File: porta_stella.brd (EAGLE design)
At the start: 113.5 x 67.5 mm, 106 parts, among them CN4 MicroUSB, IC1 74LS00D, J1 PJ-393, T1 2N3904, T2 PN3906, T3 PN3906, T4 PN3906, T5 MMUN2133LT1G, U1 TPS61090RSAR, U2 MCP73871, X1 SSW-112-02-G-Q

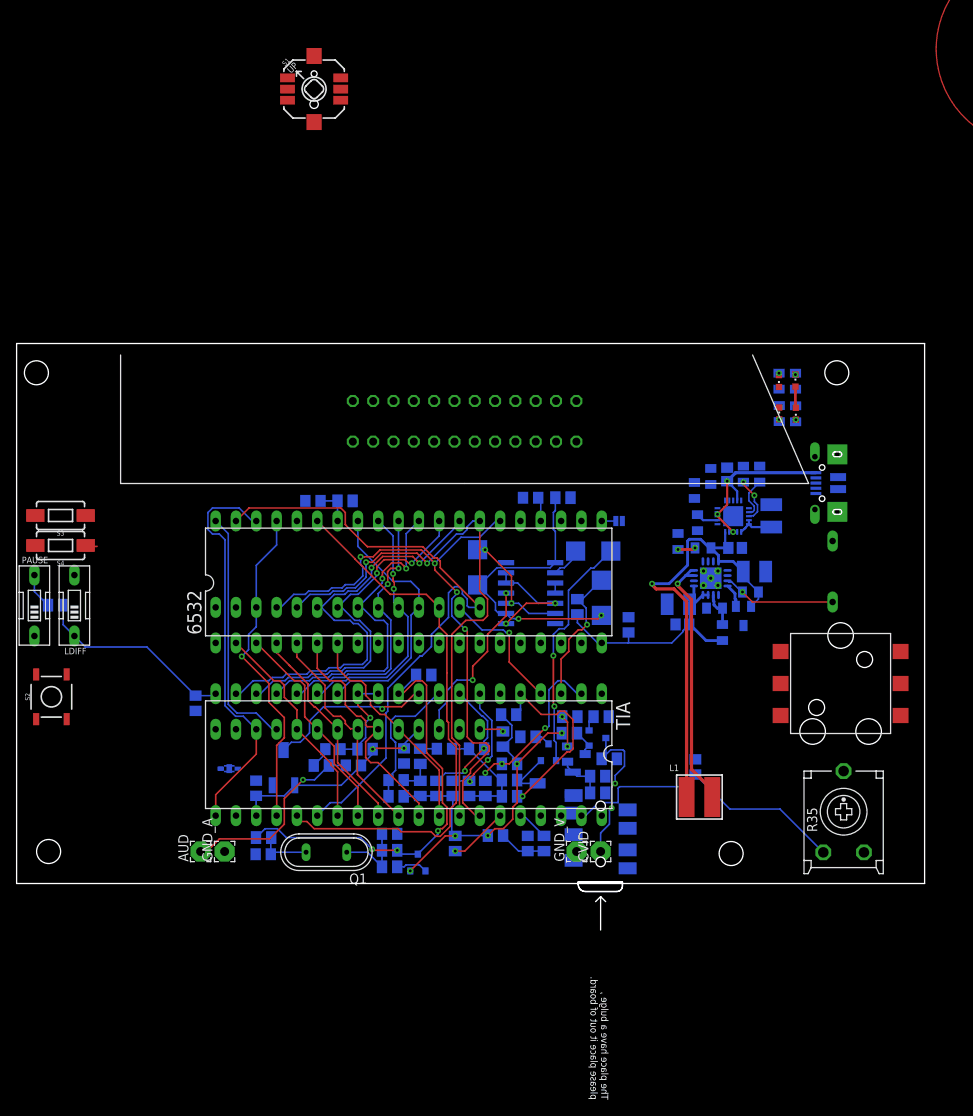
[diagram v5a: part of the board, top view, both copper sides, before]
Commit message: switched to gameboy form factor
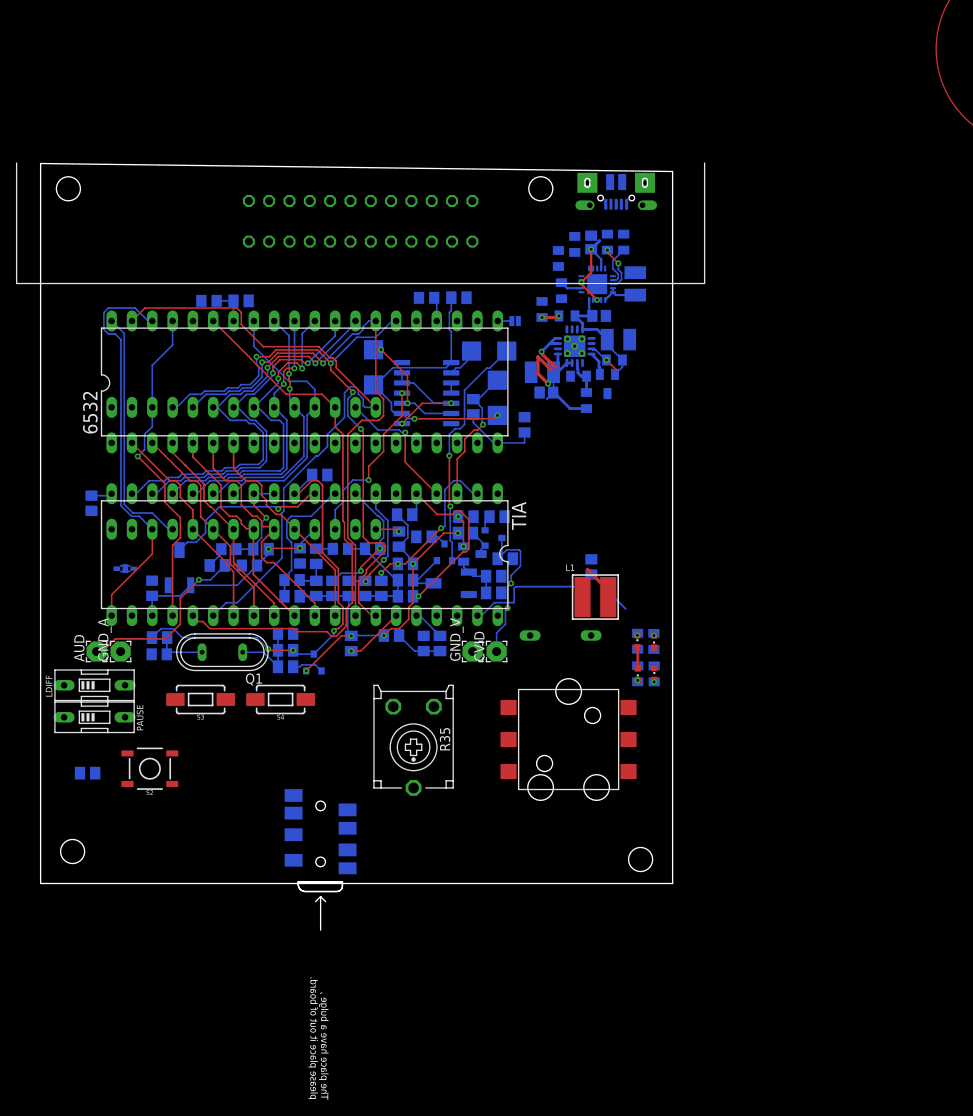
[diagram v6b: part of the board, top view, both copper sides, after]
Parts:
- removed S1: (no value), SparkFun-Switches:JOYSTICK_MINI
- moved R35 54.4 mm to (49.6, 17.0), turned to 180 degrees
- moved CN4 44.0 mm to (74.9, 85.7), turned to 180 degrees
- moved DONE 41.7 mm to (77.6, 26.1), turned to 180 degrees
- moved R45 41.6 mm to (77.6, 26.2), turned to 270 degrees
- moved ON 39.8 mm to (79.7, 26.2), turned to 0 degrees
- moved R36 39.8 mm to (79.7, 26.2), turned to 270 degrees
- moved J1 35.0 mm to (38.0, -1.00)
- moved ON/OFF1 34.9 mm to (68.0, 31.0), turned to 270 degrees
- moved U$5 34.7 mm to (69.0, 18.0)
- moved CHRG/LBO 34.7 mm to (77.6, 30.3), turned to 0 degrees
- moved R44 34.6 mm to (77.6, 30.3), turned to 90 degrees
- moved C21 33.6 mm to (77.3, 75.0)
- moved C22 33.6 mm to (71.8, 80.1)
- moved C5 33.6 mm to (75.2, 68.0)
- moved C6 33.6 mm to (66.2, 61.4)
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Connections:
- net GND: now also U$5.COM; no longer S1.GND
- net LFT_JOY_DWN: now also U$5.C-D; no longer S1.D
- net LFT_JOY_LFT: now also U$5.B-L; no longer S1.C
- net LFT_JOY_RGT: now also U$5.D-R; no longer S1.B
- net LFT_JOY_UP: now also U$5.A-U; no longer S1.A
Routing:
- net VBAT: track 56.9 -> 21.0 mm
- net +5V: track 132.8 -> 102.6 mm
- net N$10: track 32.2 -> 11.0 mm
- net LFT_PADDLE_A: track 37.5 -> 23.5 mm
- net VBUS: track 26.3 -> 16.3 mm
- net BOOST_ENABLE: track 14.2 -> 4.21 mm
- net P_SW: track 34.4 -> 30.0 mm
- net N$19: track 1.46 -> 0.00 mm
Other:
- board size 113.5 x 67.5 mm -> 79 x 90 mm

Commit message: Added new switch
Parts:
- removed LDIFF: LFT_DIFFICULTY, special:EDG-01
- removed ON/OFF1: ON/OFF, special:EDG-01
- added L_DIFF, ON/OFF: JS202011JCQN, tiny_stella:JS202011JCQN
- PAUSE: value ON/OFF -> JS202011JCQN; device special:EDG-01 -> tiny_stella:JS202011JCQN
- moved GND_V 19.2 mm to (66.0, 46.0)
- moved CVID 15.2 mm to (66.0, 43.0)
- moved S4 12.6 mm to (21.0, 27.0), turned to 270 degrees
- moved AUD 11.2 mm to (8.00, 40.0)
- moved GND_A 9.43 mm to (8.00, 37.0)
- moved S3 7.21 mm to (17.0, 27.0), turned to 270 degrees
- moved PAUSE 6.80 mm to (7.00, 27.0)
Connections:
- net BOOST_ENABLE: now also ON/OFF.P$3, ON/OFF.P$6; no longer ON/OFF1.1
- net GND: now also L_DIFF.P$1, L_DIFF.P$2, L_DIFF.P$4, L_DIFF.P$5, ON/OFF.P$1, ON/OFF.P$2, ON/OFF.P$4, ON/OFF.P$5, PAUSE.P$1, PAUSE.P$2, PAUSE.P$4, PAUSE.P$5; no longer LDIFF.1, ON/OFF1.2, PAUSE.1
- net N$21: now also L_DIFF.P$3, L_DIFF.P$6; no longer LDIFF.2
- net P_SW: now also PAUSE.P$3, PAUSE.P$6; no longer PAUSE.2
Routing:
- net N$28: track 24.5 -> 16.4 mm
- net N$25: track 20.0 -> 14.0 mm

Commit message: ready to finish wiring
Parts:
- removed GND_V: GND_V, wirepad:2,54/1,1
- removed S2: L_FIRE, SparkFun-Switches:TACTILE_SWITCH_SMD_5.2MM
- added GND_CVID: GND_CVID, wirepad:2,54/1,1
- added J2: SJ-43516-SMT, tiny_stella:CUI_SJ-43516-SMT
- added SW1: E-SWITCH_JS5208E-SWITCH_JS5208_0_0, tiny_stella:E-SWITCH_JS5208_0
- added U$7: TL3300DF260Q, tiny_stella:TL3300DF260Q
- J1: value PJ-393 -> 2p-smd-1.0-90d; device Seeed-Connector:AUDIO8P-SMD-3.5-14.5X6.1X4.0MM -> Seeed-Connector:HW2-SMD-1.0-90D
- U$5: value JS5208 -> 3352P-1-103LF; device tiny_stella:JS5208_PKG -> tiny_stella:3352P-1-103LF
- moved PAUSE 60.1 mm to (67.1, 29.5), turned to 0 degrees
- moved L_DIFF 45.5 mm to (57.4, 29.5), turned to 0 degrees
- moved J1 41.1 mm to (4.57, 22.9), turned to 0 degrees
- moved U$5 23.0 mm to (50.3, 4.57), turned to 180 degrees
- moved S3 11.3 mm to (6.02, 29.7), turned to 0 degrees
- moved S4 6.40 mm to (15.2, 29.6), turned to 0 degrees
- moved 6532 3.05 mm to (33.0, 62.7)
- moved BRIGHT 3.05 mm to (51.3, 37.5)
- moved C10 3.05 mm to (48.2, 73.2)
- moved C11 3.05 mm to (26.1, 39.8)
- moved C16 3.05 mm to (60.4, 57.3)
- moved C18 3.05 mm to (21.0, 72.8)
- moved C19 3.05 mm to (30.6, 31.2)
- moved C2 3.05 mm to (37.4, 41.8)
- moved C21 3.05 mm to (74.3, 75.0)
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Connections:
- net N$8 renamed RAW_CVID
- new net AUD: J2.2, J2.3, U$5.P$1
- new net CVID: J2.1
- new net JACK_AUD_OUT_L: J2.5
- new net JACK_AUD_OUT_R: J2.6
- new net N$56: SW1.4
- new net N$8: AUD.1
- net GND: now also GND_CVID.1, J1.-, J2.4, SW1.3, U$5.P$2, U$7.P$3, U$7.P$4; no longer GND_V.1, S2.3, U$5.COM
- net LFT_FIRE: now also U$7.P$1, U$7.P$2; no longer S2.1
- net LFT_JOY_DWN: now also SW1.2; no longer U$5.C-D
- net LFT_JOY_LFT: now also SW1.6; no longer U$5.B-L
- net LFT_JOY_RGT: now also SW1.5; no longer U$5.D-R
- net LFT_JOY_UP: now also SW1.1; no longer U$5.A-U
- net N$28: now also U$5.P$3; no longer AUD.1
- net VLIPO: now also J1.+
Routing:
- net RAW_CVID: track 14.0 -> 11.8 mm
- net +5V: vias 7 -> 6
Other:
- board size 79 x 90 mm -> 79 x 89.9 mm
